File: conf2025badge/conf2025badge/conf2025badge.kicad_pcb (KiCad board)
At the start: 2 copper layers, 100 x 70 mm, 16 parts, among them SW1 SW_PUSH, SW2 KEY_SWITCH, SW2 RotaryEncoder_Switch, SW3 SW_PUSH, U1 xiao, U2 RKJXV122400R

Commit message: Update
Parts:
- removed Ref** (x4): Val**, foostan/kbd:M2_HOLE_v2
- removed U2: RKJXV122400R, sglib:RKJXV122400R
- added H1: MountingHole, foostan/kbd:M2_HOLE_v2, F.Cu at (39.0, 24.0)
- added H2: MountingHole, foostan/kbd:M2_HOLE_v2, F.Cu at (121.0, 24.0)
- added H3: MountingHole, foostan/kbd:M2_HOLE_v2, F.Cu at (39.0, 86.0)
- added H4: MountingHole, foostan/kbd:M2_HOLE_v2, F.Cu at (121.0, 86.0)
- added R1: R, Resistor_THT:R_Axial_DIN0207_L6.3mm_D2.5mm_P10.16mm_Horizontal, F.Cu at (71.0, 24.0)
- added R2: R, Resistor_THT:R_Axial_DIN0207_L6.3mm_D2.5mm_P10.16mm_Horizontal, F.Cu at (99.0, 24.0)
- added U3: fj08k-s, sglib:FJ08K-S, F.Cu at (39.7, 59.3)
- moved BZ1 20.0 mm to (41.0, 73.0)
- moved SW2 5.00 mm to (50.0, 24.0)
- moved SW2 5.00 mm to (110.0, 24.0)
- moved SW5 2.24 mm to (110.8, 33.5)
- moved SW1 1.50 mm to (118.5, 74.0)
- moved SW3 1.50 mm to (118.5, 54.0)
- moved U1 1.00 mm to (41.0, 38.0)
- moved REF** 0.50 mm to (79.0, 71.5)
- renumbered SW2 to SW5
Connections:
- BZ1 pad 1: unconnected-(BZ1-+-Pad1) -> BUZZER
- BZ1 pad 2: unconnected-(BZ1---Pad2) -> GND
- LED1 pad 1: unconnected-(LED1-VDD-Pad1) -> 3V3
- LED1 pad 2: unconnected-(LED1-DOUT-Pad2) -> Net-(LED1-DOUT)
- LED1 pad 3: unconnected-(LED1-VSS-Pad3) -> GND
- LED1 pad 4: unconnected-(LED1-DIN-Pad4) -> SK6812MINI-E
- LED2 pad 1: unconnected-(LED2-VDD-Pad1) -> 3V3
- LED2 pad 3: unconnected-(LED2-VSS-Pad3) -> GND
- LED2 pad 4: unconnected-(LED2-DIN-Pad4) -> Net-(LED1-DOUT)
- OL1 pad 1: unconnected-(OL1-SDA-Pad1) -> SDA
- OL1 pad 2: unconnected-(OL1-SCL-Pad2) -> SCL
- OL1 pad 3: unconnected-(OL1-VCC-Pad3) -> 3V3
- OL1 pad 4: unconnected-(OL1-GND-Pad4) -> GND
- SW1 pad 1: unconnected-(SW1-Pad1) -> SW_1
- SW1 pad 2: unconnected-(SW1-Pad2) -> GND
- SW3 pad 1: unconnected-(SW3-Pad1) -> SW_2
- SW3 pad 2: unconnected-(SW3-Pad2) -> GND
- SW5 pad A: unconnected-(SW2-PadA) -> ROT_A
- SW5 pad B: unconnected-(SW2-PadB) -> ROT_B
- SW5 pad C: unconnected-(SW2-PadC) -> GND
- SW5 pad S1: unconnected-(SW2-PadS1) -> ROT_BTN
- SW5 pad S2: unconnected-(SW2-PadS2) -> GND
- U1 pad 1: unconnected-(U1-A2-Pad1) -> VR_X
- U1 pad 10: unconnected-(U1-A5_MISO-Pad10) -> ROT_B
- U1 pad 11: unconnected-(U1-A6_MOSI-Pad11) -> ROT_A
- U1 pad 12: unconnected-(U1-3V3-Pad12) -> 3V3
- U1 pad 13: unconnected-(U1-GND-Pad13) -> GND
- U1 pad 2: unconnected-(U1-A4-Pad2) -> VR_Y
- U1 pad 3: unconnected-(U1-A10-Pad3) -> SW_1
- U1 pad 4: unconnected-(U1-A11-Pad4) -> SW_2
- U1 pad 5: unconnected-(U1-A8_SDA-Pad5) -> SDA
- U1 pad 6: unconnected-(U1-A9_SCL-Pad6) -> SCL
- U1 pad 7: unconnected-(U1-B8_TX-Pad7) -> SK6812MINI-E
- U1 pad 8: unconnected-(U1-B9_RX-Pad8) -> BUZZER
- U1 pad 9: unconnected-(U1-A7_SCK-Pad9) -> ROT_BTN
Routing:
- net GND: track 0.00 -> 229.1 mm
- net 3V3: track 0.00 -> 178.2 mm, vias 0 -> 1
- net SW_1: track 0.00 -> 95.5 mm
- net ROT_BTN: track 0.00 -> 92.6 mm
- net SK6812MINI-E: track 0.00 -> 82.4 mm
- net ROT_B: track 0.00 -> 79.0 mm
- net ROT_A: track 0.00 -> 77.2 mm
- net SW_2: track 0.00 -> 73.3 mm
- net BUZZER: track 0.00 -> 66.7 mm
- net SCL: track 0.00 -> 57.9 mm
- net SDA: track 0.00 -> 54.6 mm
- net Net-(LED1-DOUT): track 0.00 -> 21.2 mm
- net VR_Y: track 0.00 -> 20.8 mm
- net VR_X: track 0.00 -> 9.00 mm
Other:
- outline, holes or cut-outs redrawn
- board text added: "JLCJLCJLCJLC"

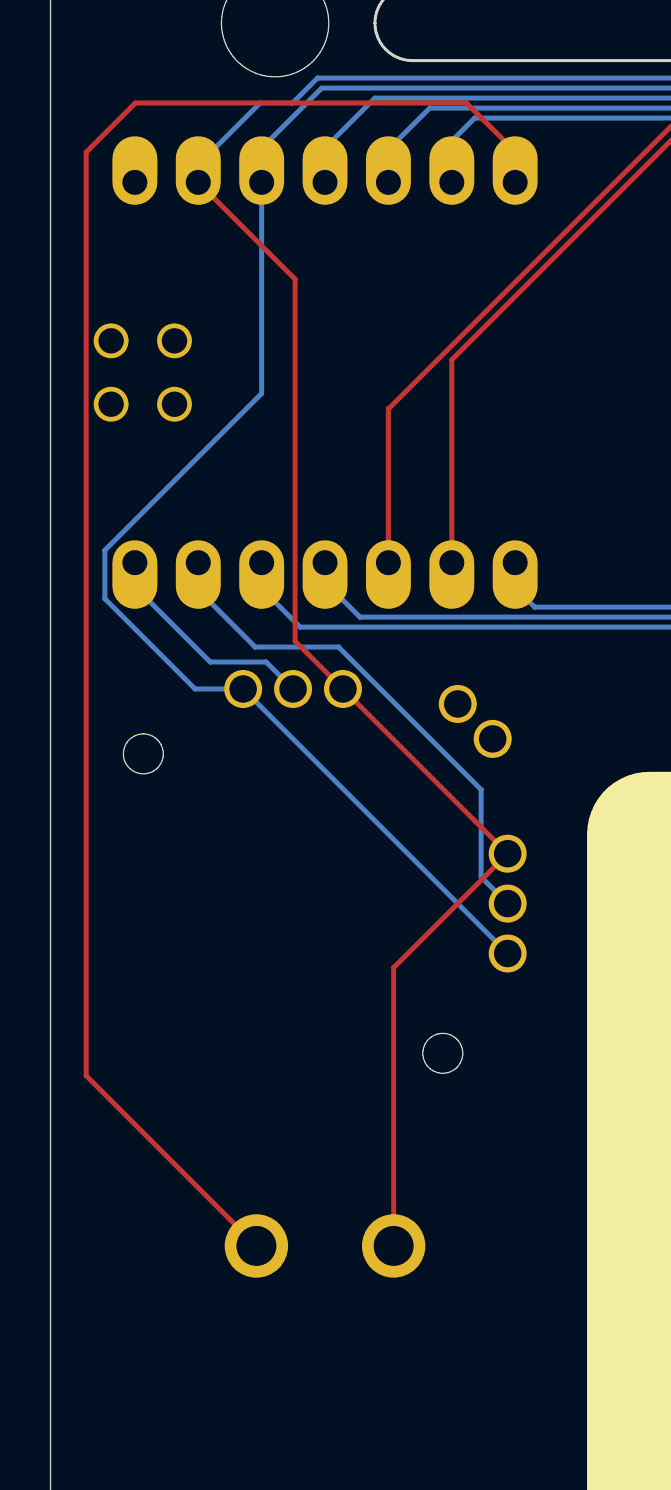
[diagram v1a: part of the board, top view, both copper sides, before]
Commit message: Update conf2025badge PCB (move buzzer down)
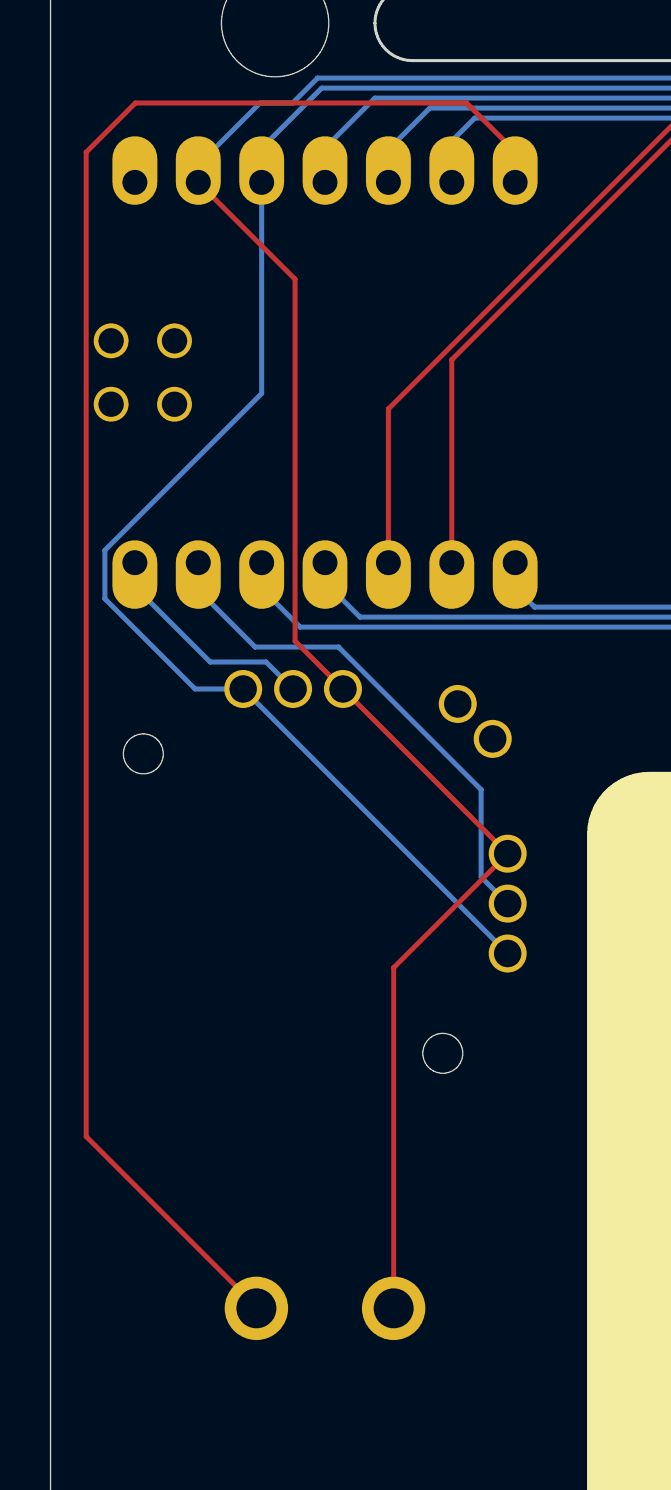
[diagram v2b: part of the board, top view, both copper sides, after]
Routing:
- net GND: track 229.1 -> 231.6 mm
- net BUZZER: track 66.7 -> 69.2 mm
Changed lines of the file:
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@@
 		)
 		(pad "1" thru_hole circle
-			(at -2.75 0)
+			(at -2.75 2.5)
 			(size 2.54 2.54)
 			(drill 1.6)
@@
 		)
 		(pad "2" thru_hole circle
-			(at 2.75 0)
+			(at 2.75 2.5)
 			(size 2.54 2.54)
 			(drill 1.6)
@@
 	)
 	(segment
-		(start 43.75 61.85)
-		(end 48.319 57.281)
-		(width 0.2)
-		(layer "F.Cu")
-		(net 1)
-	)
-	(segment
 		(start 117.95 26.2)
 		(end 125.25 33.5)
@@
 	)
 	(segment
-		(start 43.75 73)
-		(end 43.75 61.85)
-		(width 0.2)
-		(layer "F.Cu")
-		(net 1)
-	)
-	(segment
 		(start 77.44 21)
 		(end 98.2 21)
@@
 	(segment
 		(start 48.319 57.281)
+		(end 43.75 61.85)
+		(width 0.2)
+		(layer "F.Cu")
+		(net 1)
+	)
+	(segment
+		(start 48.319 57.281)
 		(end 41.719 50.681)
 		(width 0.2)
@@
 	)
 	(segment
+		(start 43.75 61.85)
+		(end 43.75 75.5)
+		(width 0.2)
+		(layer "F.Cu")
+		(net 1)
+	)
+	(segment
 		(start 126.551 34.801)
 		(end 125.25 33.5)
@@
 	)
 	(segment
-		(start 46.670308 27.2)
-		(end 33.4 27.2)
+		(start 33.4 27.2)
+		(end 31.4285 29.1715)
 		(width 0.2)
 		(layer "F.Cu")
@@
 	)
 	(segment
-		(start 31.4285 66.1785)
-		(end 38.25 73)
+		(start 38.25 75.43663)
+		(end 38.25 75.5)
 		(width 0.2)
 		(layer "F.Cu")
@@
 	)
 	(segment
-		(start 33.4 27.2)
-		(end 31.4285 29.1715)
+		(start 31.4285 68.61513)
+		(end 38.25 75.43663)
 		(width 0.2)
 		(layer "F.Cu")
@@
 	)
 	(segment
-		(start 48.62 30.38)
-		(end 48.62 29.149692)
+		(start 46.670308 27.2)
+		(end 33.4 27.2)
 		(width 0.2)
 		(layer "F.Cu")
@@
 	)
 	(segment
-		(start 31.4285 29.1715)
-		(end 31.4285 66.1785)
+		(start 48.62 30.38)
+		(end 48.62 29.149692)
 		(width 0.2)
 		(layer "F.Cu")
@@
 		(width 0.2)
 		(layer "F.Cu")
+		(net 2)
+	)
+	(segment
+		(start 31.4285 29.1715)
+		(end 31.4285 68.61513)
+		(width 0.2)
+		(layer "F.Cu")
